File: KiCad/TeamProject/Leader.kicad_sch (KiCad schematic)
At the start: 9 parts, among them SW1 Reset, U1 PIC32MX170F256B

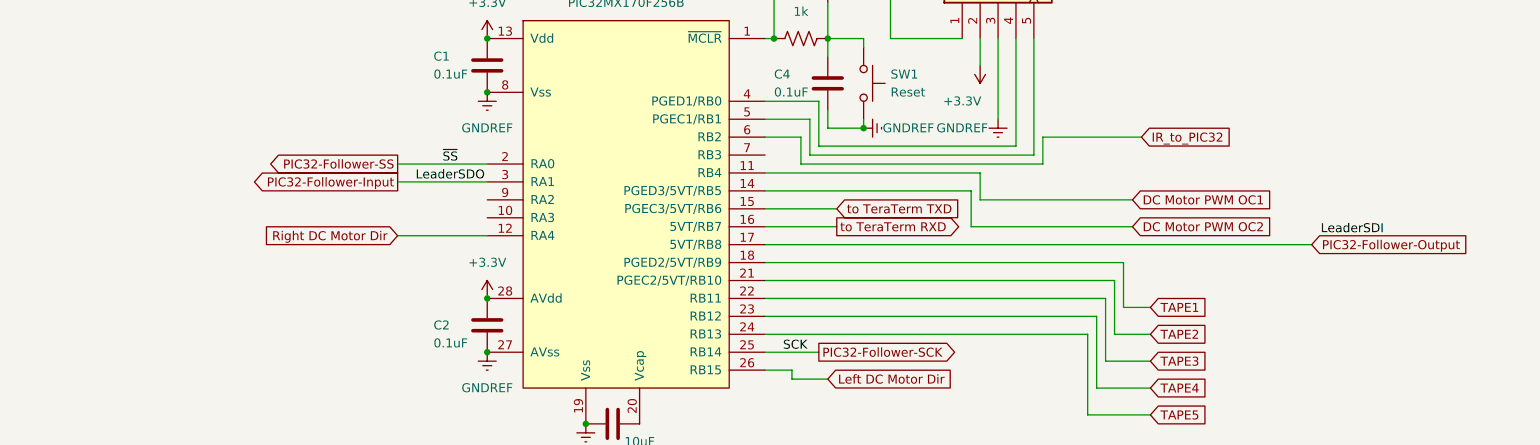
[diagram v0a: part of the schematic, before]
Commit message: Replace shooting stepper with servo, add ball lifting servo with no pin available on follower, add side indicator servo to leader
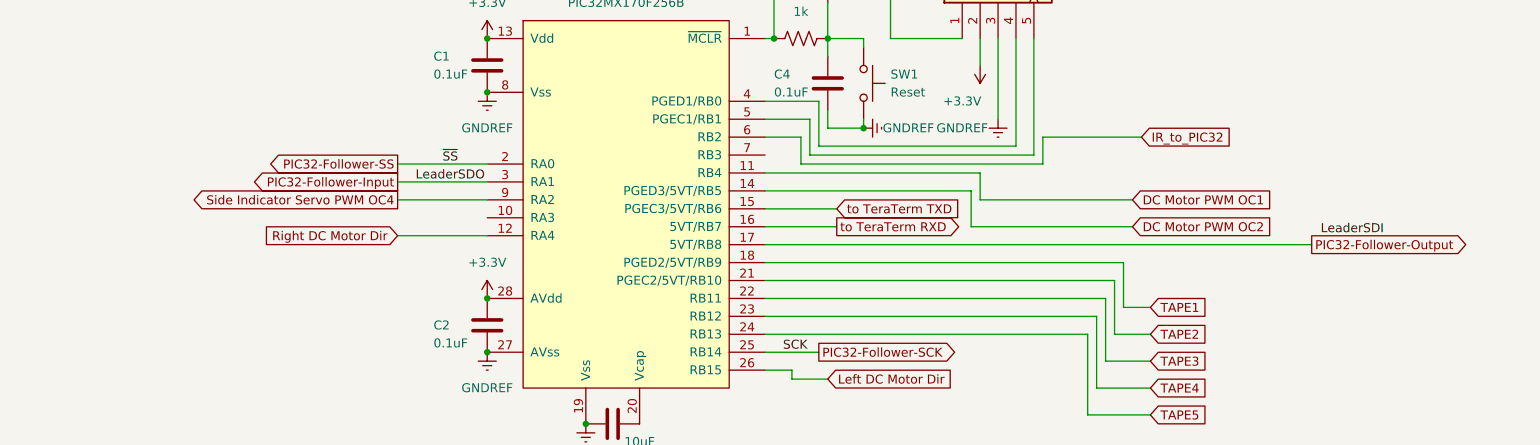
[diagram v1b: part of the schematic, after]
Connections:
- net Side Indicator Servo PWM OC4: now reaches U1.9 (RA2)
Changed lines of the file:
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@@
+	(wire
+		(pts
+			(xy 91.44 67.31) (xy 78.74 67.31)
+		)
+		(stroke
+			(width 0)
+			(type default)
+		)
+	)
 	(wire
 		(pts
@@
 	)
 	(global_label "PIC32-Follower-Output"
-		(shape input)
+		(shape output)
 		(at 208.28 73.66 0)
 		(fields_autoplaced yes)
@@
 				)
 				(justify left)
+				(hide yes)
+			)
+		)
+	)
+	(global_label "Side Indicator Servo PWM OC4"
+		(shape output)
+		(at 78.74 67.31 180)
+		(fields_autoplaced yes)
+		(effects
+			(font
+				(size 1.27 1.27)
+			)
+			(justify right)
+		)
+		(property "Intersheetrefs" "${INTERSHEET_REFS}"
+			(at 46.2427 67.31 0)
+			(effects
+				(font
+					(size 1.27 1.27)
+				)
+				(justify right)
 				(hide yes)
 			)
@@
 		)
 		(instances
-			(project "TeamProject"
+			(project "Leader"
 				(path "/e69a436c-b634-4c28-b262-47742fc47b6f"
 					(page "3")
@@
 		)
 		(instances
-			(project "TeamProject"
+			(project "Leader"
 				(path "/e69a436c-b634-4c28-b262-47742fc47b6f"
 					(page "2")

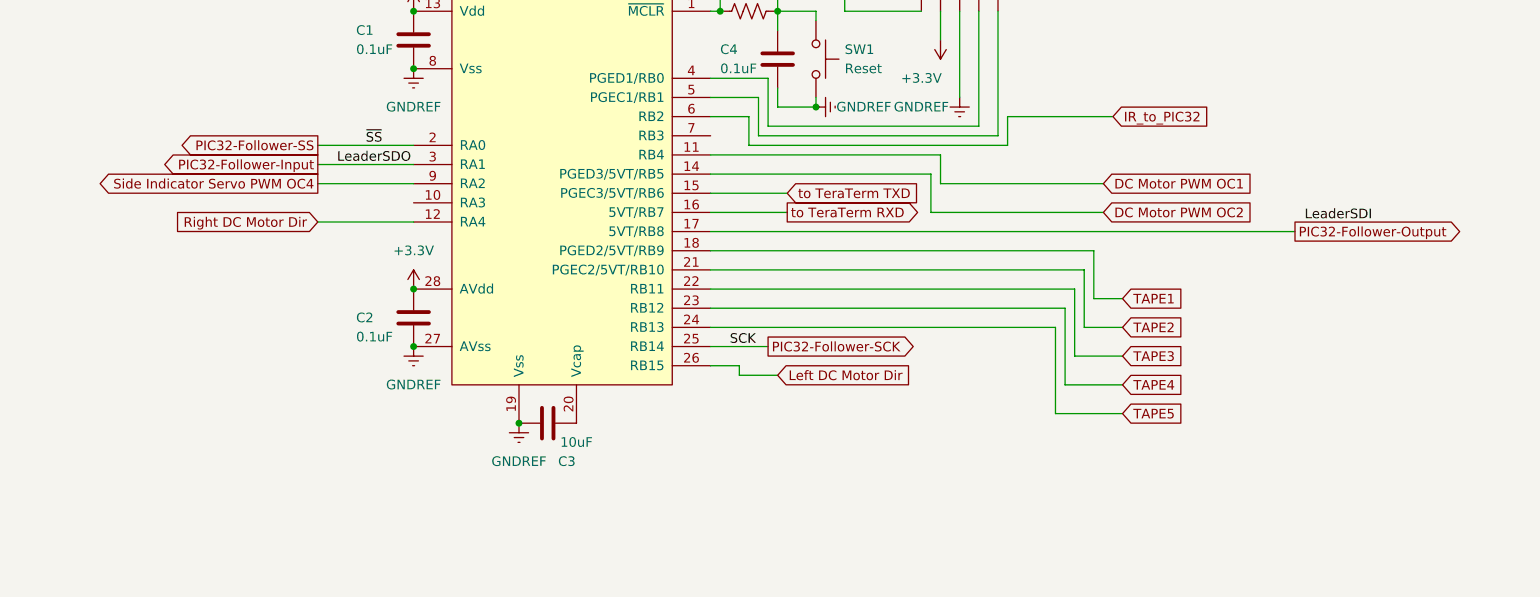
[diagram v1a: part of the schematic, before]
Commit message: Refactoring DCMotorService on LeaderPIC in progress
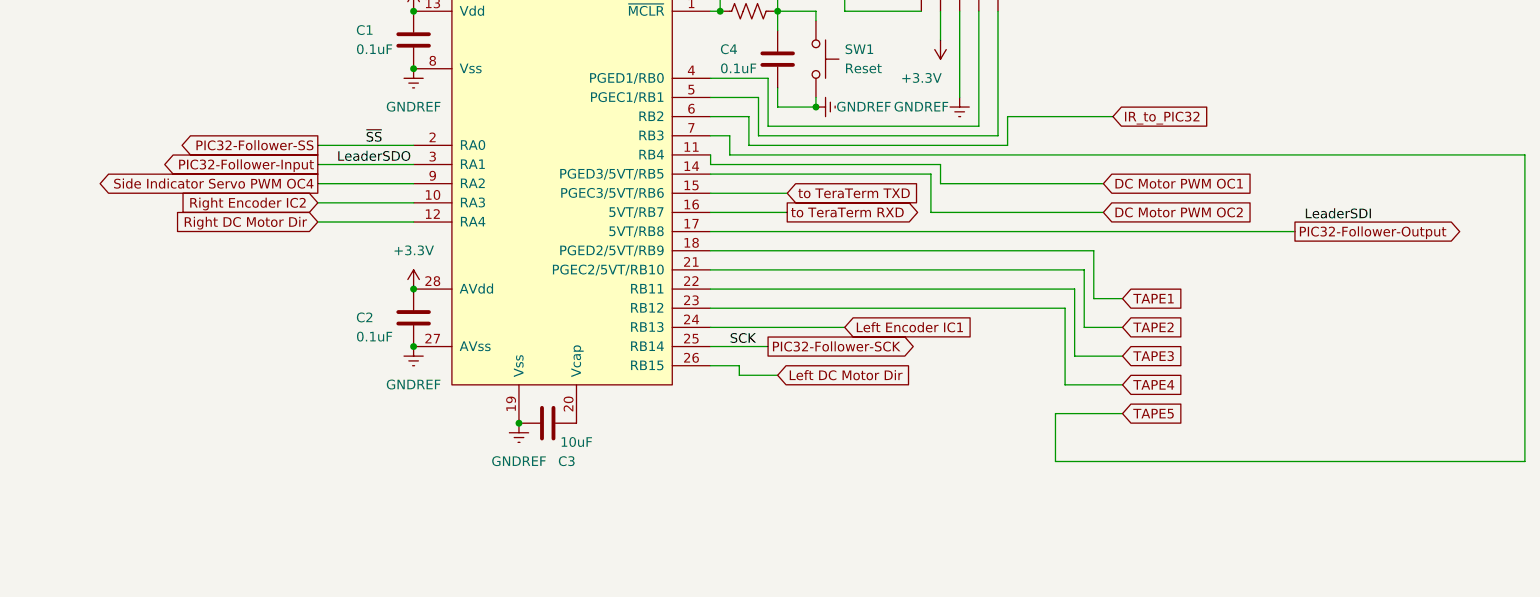
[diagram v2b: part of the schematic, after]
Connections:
- net TAPE5: now also U1.7 (RB3); no longer U1.24 (RB13)
- net Right Encoder IC2: now reaches U1.10 (RA3)
- new net Left Encoder IC1: U1.24 (RB13)
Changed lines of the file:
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@@
+	(wire
+		(pts
+			(xy 176.53 97.79) (xy 176.53 104.14)
+		)
+		(stroke
+			(width 0)
+			(type default)
+		)
+	)
 	(wire
 		(pts
@@
 	(wire
 		(pts
+			(xy 133.35 63.5) (xy 238.76 63.5)
+		)
+		(stroke
+			(width 0)
+			(type default)
+		)
+	)
+	(wire
+		(pts
+			(xy 130.81 86.36) (xy 148.59 86.36)
+		)
+		(stroke
+			(width 0)
+			(type default)
+		)
+	)
+	(wire
+		(pts
 			(xy 135.89 62.23) (xy 170.18 62.23)
 		)
@@
 	(wire
 		(pts
-			(xy 161.29 63.5) (xy 161.29 67.31)
+			(xy 161.29 64.77) (xy 161.29 67.31)
 		)
 		(stroke
@@
 	(wire
 		(pts
+			(xy 78.74 69.85) (xy 91.44 69.85)
+		)
+		(stroke
+			(width 0)
+			(type default)
+		)
+	)
+	(wire
+		(pts
 			(xy 161.29 44.45) (xy 161.29 48.26)
 		)
@@
 	(wire
 		(pts
+			(xy 238.76 104.14) (xy 238.76 63.5)
+		)
+		(stroke
+			(width 0)
+			(type default)
+		)
+	)
+	(wire
+		(pts
+			(xy 130.81 64.77) (xy 130.81 63.5)
+		)
+		(stroke
+			(width 0)
+			(type default)
+		)
+	)
+	(wire
+		(pts
 			(xy 138.43 59.69) (xy 138.43 53.34)
 		)
@@
 	(wire
 		(pts
-			(xy 130.81 63.5) (xy 161.29 63.5)
+			(xy 130.81 64.77) (xy 161.29 64.77)
 		)
 		(stroke
@@
 	(wire
 		(pts
+			(xy 133.35 63.5) (xy 133.35 60.96)
+		)
+		(stroke
+			(width 0)
+			(type default)
+		)
+	)
+	(wire
+		(pts
 			(xy 163.83 55.88) (xy 163.83 44.45)
 		)
@@
 	(wire
 		(pts
+			(xy 133.35 60.96) (xy 130.81 60.96)
+		)
+		(stroke
+			(width 0)
+			(type default)
+		)
+	)
+	(wire
+		(pts
+			(xy 176.53 104.14) (xy 238.76 104.14)
+		)
+		(stroke
+			(width 0)
+			(type default)
+		)
+	)
+	(wire
+		(pts
 			(xy 78.74 72.39) (xy 91.44 72.39)
 		)
@@
 		(pts
 			(xy 134.62 91.44) (xy 134.62 92.71)
-		)
-		(stroke
-			(width 0)
-			(type default)
-		)
-	)
-	(wire
-		(pts
-			(xy 176.53 86.36) (xy 176.53 97.79)
-		)
-		(stroke
-			(width 0)
-			(type default)
-		)
-	)
-	(wire
-		(pts
-			(xy 130.81 86.36) (xy 176.53 86.36)
 		)
 		(stroke
@@
 				(hide yes)
 			)
+		)
+	)
+	(global_label "Right Encoder IC2"
+		(shape input)
+		(at 78.74 69.85 180)
+		(fields_autoplaced yes)
+		(effects
+			(font
+				(size 1.27 1.27)
+			)
+			(justify right)
+		)
+		(property "Intersheetrefs" "${INTERSHEET_REFS}"
+			(at 58.2774 69.85 0)
+			(effects
+				(font
+					(size 1.27 1.27)
+				)
+				(justify right)
+				(hide yes)
+			)
+		)
+	)
+	(global_label "Left Encoder IC1"
+		(shape input)
+		(at 148.59 86.36 0)
+		(fields_autoplaced yes)
+		(effects
+			(font
+				(size 1.27 1.27)
+			)
+			(justify left)
+		)
+		(property "Intersheetrefs" "${INTERSHEET_REFS}"
+			(at 167.7222 86.36 0)
+			(effects
+				(font
+					(size 1.27 1.27)
+				)
+				(justify left)
+				(hide yes)
+			)

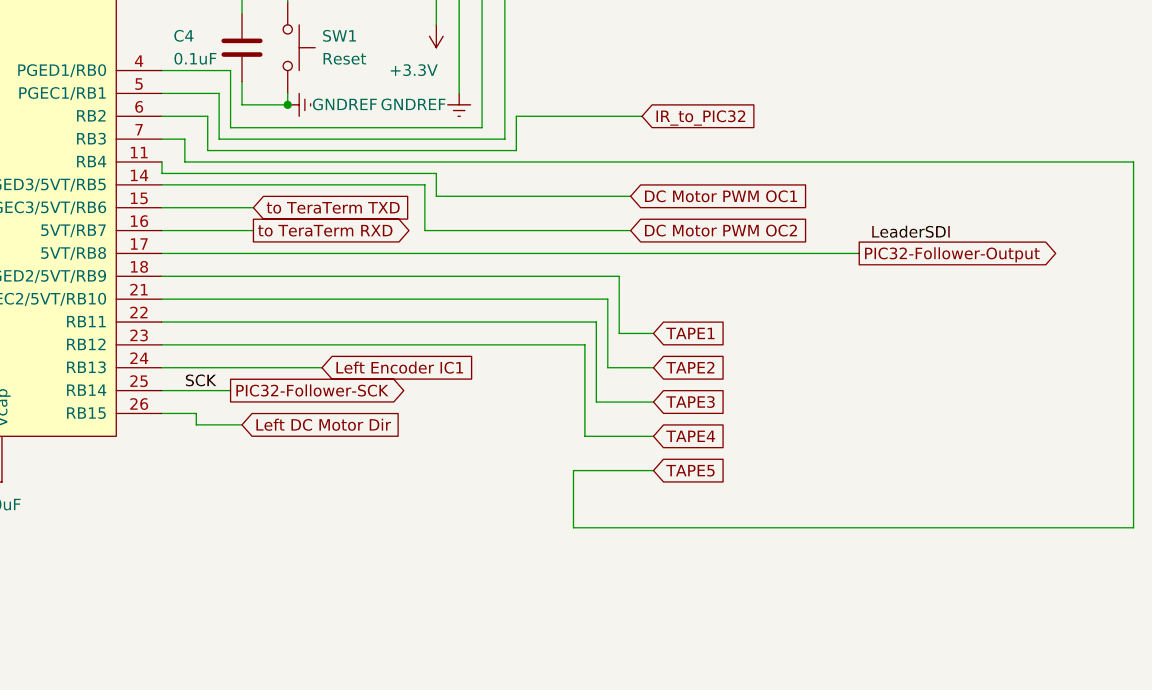
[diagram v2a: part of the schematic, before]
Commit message: Update tape detector code in DCMotorService
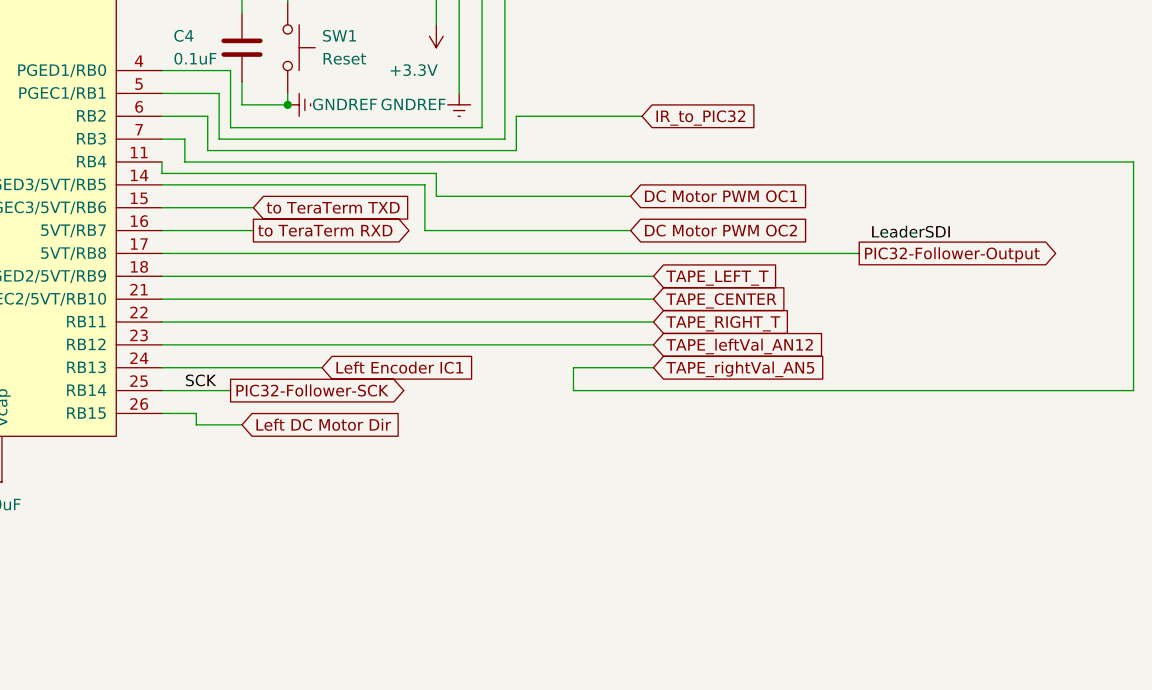
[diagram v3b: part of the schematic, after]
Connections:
- net TAPE1 renamed TAPE_LEFT_T
- net TAPE2 renamed TAPE_CENTER
- net TAPE3 renamed TAPE_RIGHT_T
- net TAPE4 renamed TAPE_leftVal_AN12
- net TAPE5 renamed TAPE_rightVal_AN5
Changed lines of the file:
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@@
 	(wire
 		(pts
-			(xy 176.53 97.79) (xy 176.53 104.14)
+			(xy 176.53 86.36) (xy 176.53 88.9)
 		)
 		(stroke
@@
 	(wire
 		(pts
-			(xy 181.61 76.2) (xy 181.61 82.55)
-		)
-		(stroke
-			(width 0)
-			(type default)
-		)
-	)
-	(wire
-		(pts
-			(xy 176.53 97.79) (xy 185.42 97.79)
+			(xy 130.81 78.74) (xy 185.42 78.74)
+		)
+		(stroke
+			(width 0)
+			(type default)
+		)
+	)
+	(wire
+		(pts
+			(xy 176.53 86.36) (xy 185.42 86.36)
 		)
 		(stroke
@@
 	(wire
 		(pts
-			(xy 181.61 82.55) (xy 185.42 82.55)
-		)
-		(stroke
-			(width 0)
-			(type default)
-		)
-	)
-	(wire
-		(pts
 			(xy 158.75 44.45) (xy 148.59 44.45)
 		)
@@
 	(wire
 		(pts
-			(xy 179.07 90.17) (xy 185.42 90.17)
-		)
-		(stroke
-			(width 0)
-			(type default)
-		)
-	)
-	(wire
-		(pts
 			(xy 130.81 91.44) (xy 134.62 91.44)
 		)
@@
 	(wire
 		(pts
-			(xy 130.81 83.82) (xy 177.8 83.82)
+			(xy 130.81 83.82) (xy 185.42 83.82)
 		)
 		(stroke
@@
 	(wire
 		(pts
-			(xy 177.8 93.98) (xy 185.42 93.98)
-		)
-		(stroke
-			(width 0)
-			(type default)
-		)
-	)
-	(wire
-		(pts
 			(xy 91.44 67.31) (xy 78.74 67.31)
 		)
@@
 	(wire
 		(pts
-			(xy 238.76 104.14) (xy 238.76 63.5)
+			(xy 238.76 88.9) (xy 238.76 63.5)
 		)
 		(stroke
@@
 	(wire
 		(pts
-			(xy 130.81 81.28) (xy 179.07 81.28)
+			(xy 130.81 81.28) (xy 185.42 81.28)
+		)
+		(stroke
+			(width 0)
+			(type default)
+		)
+	)
+	(wire
+		(pts
+			(xy 130.81 76.2) (xy 185.42 76.2)
 		)
 		(stroke
@@
 	(wire
 		(pts
-			(xy 180.34 86.36) (xy 185.42 86.36)
-		)
-		(stroke
-			(width 0)
-			(type default)
-		)
-	)
-	(wire
-		(pts
 			(xy 132.08 20.32) (xy 132.08 44.45)
 		)
@@
 	(wire
 		(pts
-			(xy 177.8 83.82) (xy 177.8 93.98)
-		)
-		(stroke
-			(width 0)
-			(type default)
-		)
-	)
-	(wire
-		(pts
 			(xy 78.74 62.23) (xy 91.44 62.23)
 		)
@@
 	(wire
 		(pts
-			(xy 176.53 104.14) (xy 238.76 104.14)
+			(xy 176.53 88.9) (xy 238.76 88.9)
 		)
 		(stroke
@@
 		(pts
 			(xy 168.91 60.96) (xy 137.16 60.96)
-		)
-		(stroke
-			(width 0)
-			(type default)
-		)
-	)
-	(wire
-		(pts
-			(xy 179.07 81.28) (xy 179.07 90.17)
-		)
-		(stroke
-			(width 0)
-			(type default)
-		)
-	)
-	(wire
-		(pts
-			(xy 130.81 78.74) (xy 180.34 78.74)
-		)
-		(stroke
-			(width 0)
-			(type default)
-		)
-	)
-	(wire
-		(pts
-			(xy 130.81 76.2) (xy 181.61 76.2)
-		)
-		(stroke
-			(width 0)
-			(type default)
-		)
-	)
-	(wire
-		(pts
-			(xy 180.34 78.74) (xy 180.34 86.36)
 		)
 		(stroke
@@
 		)
 	)
-	(global_label "TAPE2"
-		(shape input)
-		(at 185.42 86.36 0)
-		(fields_autoplaced yes)
-		(effects
-			(font
-				(size 1.27 1.27)
-			)
-			(justify left)
-		)
-		(property "Intersheetrefs" "${INTERSHEET_REFS}"
-			(at 194.0899 86.36 0)
+	(global_label "TAPE_LEFT_T"
+		(shape input)
+		(at 185.42 76.2 0)
+		(fields_autoplaced yes)
+		(effects
+			(font
+				(size 1.27 1.27)
+			)
+			(justify left)
+		)
+		(property "Intersheetrefs" "${INTERSHEET_REFS}"
+			(at 200.0165 76.2 0)
 			(effects
 				(font
@@
 		)
 	)
-	(global_label "TAPE3"
-		(shape input)
-		(at 185.42 90.17 0)
-		(fields_autoplaced yes)
-		(effects
-			(font
-				(size 1.27 1.27)
-			)
-			(justify left)
-		)
-		(property "Intersheetrefs" "${INTERSHEET_REFS}"
-			(at 194.0899 90.17 0)
+	(global_label "TAPE_RIGHT_T"
+		(shape input)
+		(at 185.42 81.28 0)
+		(fields_autoplaced yes)
+		(effects
+			(font
+				(size 1.27 1.27)
+			)
+			(justify left)
+		)
+		(property "Intersheetrefs" "${INTERSHEET_REFS}"
+			(at 201.2261 81.28 0)
 			(effects
 				(font
@@
 		)
 	)
-	(global_label "TAPE1"
-		(shape input)
-		(at 185.42 82.55 0)
-		(fields_autoplaced yes)
-		(effects
-			(font
-				(size 1.27 1.27)
-			)
-			(justify left)
-		)
-		(property "Intersheetrefs" "${INTERSHEET_REFS}"
-			(at 194.0899 82.55 0)
-			(effects
-				(font
-					(size 1.27 1.27)
-				)
-				(justify left)
-				(hide yes)
-			)
-		)
-	)
-	(global_label "TAPE4"
-		(shape input)
-		(at 185.42 93.98 0)
-		(fields_autoplaced yes)
-		(effects
-			(font
-				(size 1.27 1.27)
-			)
-			(justify left)
-		)
-		(property "Intersheetrefs" "${INTERSHEET_REFS}"
-			(at 194.0899 93.98 0)
+	(global_label "TAPE_CENTER"
+		(shape input)
+		(at 185.42 78.74 0)
+		(fields_autoplaced yes)
+		(effects
+			(font
+				(size 1.27 1.27)
+			)
+			(justify left)
+		)
+		(property "Intersheetrefs" "${INTERSHEET_REFS}"
+			(at 200.9841 78.74 0)
+			(effects
+				(font
+					(size 1.27 1.27)
+				)
+				(justify left)
+				(hide yes)
+			)
+		)
+	)
+	(global_label "TAPE_leftVal_AN12"
+		(shape input)
+		(at 185.42 83.82 0)
+		(fields_autoplaced yes)
+		(effects
+			(font
+				(size 1.27 1.27)
+			)
+			(justify left)
+		)
+		(property "Intersheetrefs" "${INTERSHEET_REFS}"
+			(at 205.7617 83.82 0)
 			(effects
 				(font
@@
 		)
 	)
-	(global_label "TAPE5"
-		(shape input)
-		(at 185.42 97.79 0)
-		(fields_autoplaced yes)
-		(effects
-			(font
-				(size 1.27 1.27)
-			)
-			(justify left)
-		)
-		(property "Intersheetrefs" "${INTERSHEET_REFS}"
-			(at 194.0899 97.79 0)
-			(effects
-				(font
+	(global_label "TAPE_rightVal_AN5"
+		(shape input)
+		(at 185.42 86.36 0)
+		(fields_autoplaced yes)
+		(effects
+			(font
+				(size 1.27 1.27)
+			)
+			(justify left)
+		)
+		(property "Intersheetrefs" "${INTERSHEET_REFS}"
+			(at 205.7617 86.36 0)
+			(effects
+				(font

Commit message: Update connection for leader pic
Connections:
- net TAPE_rightVal_AN5 is gone; now on net TAPE_CENTER: U1.7 (RB3)
- net Left Encoder IC1: now also U1.22 (RB11); no longer U1.24 (RB13)
- net TAPE_CENTER: no longer U1.21 (PGEC2/5VT/RB10)
- net TAPE_RIGHT_T: now also U1.21 (PGEC2/5VT/RB10); no longer U1.22 (RB11)
- new net TAPE_rightVal_AN11: U1.24 (RB13)
